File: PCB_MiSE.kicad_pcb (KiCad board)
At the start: 2 copper layers, 75 x 80.2 mm, 40 parts, among them IC1 MSP430FR2355TPT, J1 WIFI, J10 Conn_01x01, J11 Conn_01x01, J2 Conn_01x03, J3 Conn_01x01, J4 Clk read conn, J5 Conn_01x01, J6 Display, J7 Conn_01x01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

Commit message: MiSE 13/3
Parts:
- R1, R10, R5, R9: value R -> 10k
- R12, R13: value R -> 2k2
- R14, R6, R7: value R -> 1k
- R2: value R -> 31k
- R3: value R -> 20k
- R4: value R -> 47k
- moved SW1 73.1 mm to (65.5, 114.2), turned to 90 degrees
- moved C1 72.3 mm to (72.5, 111.0)
- moved R4 72.3 mm to (75.5, 111.1)
- moved R6 68.4 mm to (94.0, 43.6)
- moved SW2 67.6 mm to (82.2, 41.4), turned to 0 degrees
- moved J7 58.3 mm to (76.2, 115.0)
- moved J11 12.4 mm to (47.6, 100.8)
- moved R10 11.4 mm to (51.9, 99.0), turned to 90 degrees
- moved J1 9.99 mm to (46.3, 88.3)
- moved J10 8.01 mm to (54.6, 88.8)
- moved R5 3.25 mm to (80.8, 100.5), turned to 180 degrees
- moved C3 1.76 mm to (80.8, 94.7), turned to -90 degrees
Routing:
- net TDO/TDI: track 139.2 -> 52.6 mm, vias 3 -> 2
- net Net-(IC1-P3.4/SMCLK): track 24.7 -> 84.3 mm, vias 0 -> 1
- net U0TXD: track 50.7 -> 20.6 mm, vias 3 -> 1
- net GND: track 47.7 -> 54.4 mm
- net U0RXD: track 35.9 -> 29.2 mm, vias 2 -> 1
- net CH_EN: track 10.8 -> 5.95 mm
- net Net-(IC1-P3.1/OA2O): track 40.2 -> 37.7 mm
- net GPIOr': track 22.9 -> 23.5 mm

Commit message: Final para Gerber
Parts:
- moved J7 30.3 mm to (47.5, 105.2)
- moved J2 1.71 mm to (78.0, 105.0)
- moved R5 1.03 mm to (80.1, 101.2)
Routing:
- net TDO/TDI: track 52.6 -> 59.7 mm
- net TCK: track 18.5 -> 20.2 mm
- net Net-(IC1-P1.1/UCB0CLK/ACLK/OA0O/COMP0.1/A1): track 44.1 -> 45.1 mm
- net Net-(IC1-P3.1/OA2O): track 37.7 -> 37.0 mm
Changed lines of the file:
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@@
 	(footprint "Connector_PinHeader_2.54mm:PinHeader_1x03_P2.54mm_Vertical"
 		(layer "F.Cu")
-		(at 77.9 103.35 90)
+		(at 78.04 105.05 90)
 		(descr "Through hole straight pin header, 1x03, 2.54mm pitch, single row")
 		(tags "Through hole pin header THT 1x03 2.54mm single row")
@@
 	(footprint "Resistor_SMD:R_0805_2012Metric_Pad1.20x1.40mm_HandSolder"
 		(layer "F.Cu")
-		(at 80.85 100.5 180)
+		(at 80.08 101.19 180)
 		(descr "Resistor SMD 0805 (2012 Metric), square (rectangular) end terminal, IPC-7351 nominal with elongated pad for handsoldering. (Body size source: IPC-SM-782 page 72, https://www.pcb-3d.com/wordpress/wp-content/uploads/ipc-sm-782a_amendment_1_and_2.pdf), generated with kicad-footprint-generator")
 		(tags "resistor handsolder")
@@
 	(footprint "Connector_PinHeader_2.54mm:PinHeader_1x01_P2.54mm_Vertical"
 		(layer "F.Cu")
-		(at 76.25 114.95 90)
+		(at 47.53 105.19 90)
 		(descr "Through hole straight pin header, 1x01, 2.54mm pitch, single row")
 		(tags "Through hole pin header THT 1x01 2.54mm single row")
@@
 		(tags "Switch")
 		(property "Reference" "S1"
-			(at -2.85 7.755 0)
+			(at -1.905 3.995 0)
 			(layer "F.SilkS")
 			(effects
@@
 	)
 	(segment
+		(start 79.72 109.61)
+		(end 81.06 109.61)
+		(width 0.5)
+		(layer "F.Cu")
+		(net 13)
+	)
+	(segment
 		(start 69.95 114.2)
 		(end 69.95 107.7)
@@
 	)
 	(segment
-		(start 72.55 110.0125)
-		(end 75.4 110.0125)
+		(start 83.12 107.55)
+		(end 83.12 105.05)
 		(width 0.5)
 		(layer "F.Cu")
@@
 	)
 	(segment
-		(start 78.65 107.68)
-		(end 82.98 103.35)
+		(start 72.55 110.0125)
+		(end 75.4 110.0125)
 		(width 0.5)
 		(layer "F.Cu")
@@
 		(net 13)
 	)
+	(segment
+		(start 81.06 109.61)
+		(end 83.12 107.55)
+		(width 0.5)
+		(layer "F.Cu")
+		(net 13)
+	)
 	(via
-		(at 78.65 107.68)
+		(at 79.72 109.61)
 		(size 1)
 		(drill 0.6)
@@
 	)
 	(segment
-		(start 71.851 95.301)
-		(end 68.9 92.35)
+		(start 69.95 107.7)
+		(end 71.82 109.57)
 		(width 0.5)
 		(layer "B.Cu")
@@
 	)
 	(segment
-		(start 82.98 103.35)
-		(end 81.679 104.651)
+		(start 83.12 106.58)
+		(end 83.12 105.05)
 		(width 0.5)
 		(layer "B.Cu")
@@
 	)
 	(segment
-		(start 76.599 104.651)
-		(end 71.851 99.903)
+		(start 71.851 95.301)
+		(end 71.851 103.131)
 		(width 0.5)
 		(layer "B.Cu")
@@
 	)
 	(segment
-		(start 78.65 107.7)
-		(end 69.95 107.7)
+		(start 81.82 107.88)
+		(end 83.12 106.58)
 		(width 0.5)
 		(layer "B.Cu")
@@
 	)
 	(segment
-		(start 71.851 99.903)
-		(end 71.851 95.301)
+		(start 71.851 103.131)
+		(end 76.6 107.88)
+		(width 0.5)
+		(layer "B.Cu")
+		(net 13)
+	)
+	(segment
+		(start 79.68 109.57)
+		(end 79.72 109.61)
 		(width 0.5)
 		(layer "B.Cu")
@@
 	)
 	(segment
-		(start 78.83 107.5)
-		(end 78.65 107.68)
+		(start 68.9 92.35)
+		(end 71.851 95.301)
 		(width 0.5)
 		(layer "B.Cu")
@@
 	)
 	(segment
-		(start 81.679 104.651)
-		(end 76.599 104.651)
+		(start 71.82 109.57)
+		(end 79.68 109.57)
 		(width 0.5)
 		(layer "B.Cu")
@@
 	)
 	(segment
-		(start 78.85 107.5)
-		(end 78.83 107.5)
+		(start 76.6 107.88)
+		(end 81.82 107.88)
 		(width 0.5)
 		(layer "B.Cu")
@@
 	)
 	(segment
+		(start 79.225 100.185)
+		(end 80.57 101.53)
+		(width 0.5)
+		(layer "B.Cu")
+		(net 18)
+	)
+	(segment
 		(start 74.95 100.175)
 		(end 79.225 100.175)
@@
 	)
 	(segment
+		(start 80.58 103.46)
+		(end 80.58 105.05)
+		(width 0.5)
+		(layer "B.Cu")
+		(net 18)
+	)
+	(segment
+		(start 80.57 101.53)
+		(end 80.57 103.45)
+		(width 0.5)
+		(layer "B.Cu")
+		(net 18)
+	)
+	(segment
 		(start 79.225 100.175)
-		(end 80.74 101.69)
+		(end 79.225 100.185)
 		(width 0.5)
 		(layer "B.Cu")
@@
 	)
 	(segment
-		(start 80.74 101.69)
-		(end 80.74 103.3)
+		(start 80.57 103.45)
+		(end 80.58 103.46)
 		(width 0.5)
 		(layer "B.Cu")
@@
 	)
 	(segment
-		(start 106.84 113.8)
-		(end 103.44 110.4)
+		(start 72.85 94.45)
+		(end 72.8 94.45)
 		(width 0.5)
 		(layer "B.Cu")
@@
 	)
 	(segment
-		(start 72.85 94.45)
-		(end 72.8 94.45)
+		(start 81.35 95.2)
+		(end 73.6 95.2)
 		(width 0.5)
 		(layer "B.Cu")
@@
 	)
 	(segment
-		(start 103.44 110.4)
-		(end 96.55 110.4)
+		(start 106.84 112.01)
+		(end 105.23 110.4)
 		(width 0.5)
 		(layer "B.Cu")
@@
 	)
 	(segment
-		(start 96.55 110.4)
-		(end 81.35 95.2)
+		(start 105.23 110.4)
+		(end 96.55 110.4)
 		(width 0.5)
 		(layer "B.Cu")
@@
 	)
 	(segment
-		(start 81.35 95.2)
-		(end 73.6 95.2)
+		(start 106.84 113.8)
+		(end 106.84 112.01)
+		(width 0.5)
+		(layer "B.Cu")
+		(net 19)
+	)
+	(segment
+		(start 96.55 110.4)
+		(end 81.35 95.2)
 		(width 0.5)
 		(layer "B.Cu")
@@
 	)
 	(segment
-		(start 68.6 98.55)
-		(end 68.6 95.796)
-		(width 0.25)
-		(layer "F.Cu")
-		(net 23)
-	)
-	(segment
-		(start 75.1 102)
-		(end 76.6 100.5)
+		(start 71.19 101.14)
+		(end 79.08 101.14)
 		(width 0.5)
 		(layer "F.Cu")
@@
 	)
 	(segment
-		(start 90.65 105.5)
-		(end 94.7 105.5)
-		(width 0.5)
-		(layer "F.Cu")
-		(net 23)
-	)
-	(segment
-		(start 72.05 102)
-		(end 75.1 102)
-		(width 0.5)
-		(layer "F.Cu")
-		(net 23)
-	)
-	(segment
-		(start 86.801 101.651)
-		(end 81.001 101.651)
-		(width 0.5)
+		(start 68.6 98.55)
+		(end 68.6 95.796)
+		(width 0.25)
 		(layer "F.Cu")
 		(net 23)
 	)
 	(segment
-		(start 76.6 100.5)
-		(end 79.85 100.5)
+		(start 91.92 102.72)
+		(end 98.025 108.825)
 		(width 0.5)
 		(layer "F.Cu")
@@
 	)
 	(segment
-		(start 81.001 101.651)
-		(end 79.85 100.5)
+		(start 79.08 102.17)
+		(end 79.63 102.72)
 		(width 0.5)
 		(layer "F.Cu")
@@
 	)
 	(segment
-		(start 90.65 105.5)
-		(end 86.801 101.651)
+		(start 79.63 102.72)
+		(end 91.92 102.72)
 		(width 0.5)
 		(layer "F.Cu")
@@
 	)
 	(segment
-		(start 94.7 105.5)
-		(end 98.025 108.825)
+		(start 79.08 101.14)
+		(end 79.08 102.17)
 		(width 0.5)
 		(layer "F.Cu")
@@
 	(segment
 		(start 70.1 100.05)
-		(end 72.05 102)
+		(end 71.19 101.14)
 		(width 0.5)
 		(layer "F.Cu")

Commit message: Final para Gerber
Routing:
- net U0RXD: track 29.2 -> 22.9 mm
- net Net-(IC1-P3.4/SMCLK): track 84.3 -> 86.6 mm
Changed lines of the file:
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@@
 	)
 	(segment
-		(start 53.65 78.675)
+		(start 48 84.325)
+		(end 48.655 84.325)
+		(width 0.75)
+		(layer "B.Cu")
+		(net 1)
+	)
+	(segment
+		(start 48.655 84.325)
+		(end 53.65 79.33)
+		(width 0.75)
+		(layer "B.Cu")
+		(net 1)
+	)
+	(segment
+		(start 53.65 79.33)
 		(end 53.65 69.25)
 		(width 0.75)
@@
 	)
 	(segment
-		(start 48 84.325)
-		(end 53.65 78.675)
-		(width 0.75)
-		(layer "B.Cu")
-		(net 1)
-	)
-	(segment
 		(start 74.208 91.808)
 		(end 71.088 91.808)
@@
 	)
 	(segment
-		(start 95.976 64.474)
-		(end 95.976 48.726)
+		(start 97.12 63.33)
+		(end 97.12 47.55)
+		(width 0.5)
+		(layer "B.Cu")
+		(net 24)
+	)
+	(segment
+		(start 90.97 41.4)
+		(end 88.65 41.4)
+		(width 0.5)
+		(layer "B.Cu")
+		(net 24)
+	)
+	(segment
+		(start 70.4 90.05)
+		(end 97.12 63.33)
+		(width 0.5)
+		(layer "B.Cu")
+		(net 24)
+	)
+	(segment
+		(start 97.12 47.55)
+		(end 90.97 41.4)
 		(width 0.5)
 		(layer "B.Cu")
@@
 	)
 	(segment
-		(start 95.976 48.726)
-		(end 88.65 41.4)
-		(width 0.5)
-		(layer "B.Cu")
-		(net 24)
-	)
-	(segment
-		(start 70.4 90.05)
-		(end 95.976 64.474)
-		(width 0.5)
-		(layer "B.Cu")
-		(net 24)
-	)
-	(segment
 		(start 60.55 104)
 		(end 63.1 104)
@@
 	)
 	(segment
+		(start 55.305 90.975)
+		(end 58.775 90.975)
+		(width 0.5)
+		(layer "B.Cu")
+		(net 37)
+	)
+	(segment
 		(start 54.6 88.85)
 		(end 51.9 86.15)
@@
 	)
 	(segment
-		(start 50.149 86.999)
-		(end 47.561 86.999)
+		(start 50.17 86.15)
+		(end 48.41 86.15)
 		(width 0.5)
 		(layer "B.Cu")
@@
 	)
 	(segment
-		(start 58.775 90.975)
-		(end 54.125 90.975)
+		(start 54.6 90.27)
+		(end 55.305 90.975)
+		(width 0.5)
+		(layer "B.Cu")
+		(net 37)
+	)
+	(segment
+		(start 48.41 86.15)
+		(end 47.17 86.15)
 		(width 0.5)
 		(layer "B.Cu")
@@
 	)
 	(segment
-		(start 47.561 86.999)
+		(start 46.26 87.06)
 		(end 46.26 88.3)
 		(width 0.5)
@@
 	)
 	(segment
-		(start 48.41 86.15)
-		(end 46.26 88.3)
+		(start 47.17 86.15)
+		(end 46.26 87.06)
 		(width 0.5)
 		(layer "B.Cu")
@@
 	)
 	(segment
-		(start 54.125 90.975)
-		(end 50.149 86.999)
-		(width 0.5)
-		(layer "B.Cu")
+		(start 54.6 88.85)
+		(end 54.6 90.27)
+		(width 0.5)
+		(layer "B.Cu")

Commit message: Final para Gerber
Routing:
- net U0RXD: track 22.9 -> 21.1 mm
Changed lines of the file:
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@@
-	)
-	(segment
-		(start 50.17 86.15)
-		(end 48.41 86.15)
-		(width 0.5)
-		(layer "B.Cu")
-		(net 37)
 	)
 	(segment

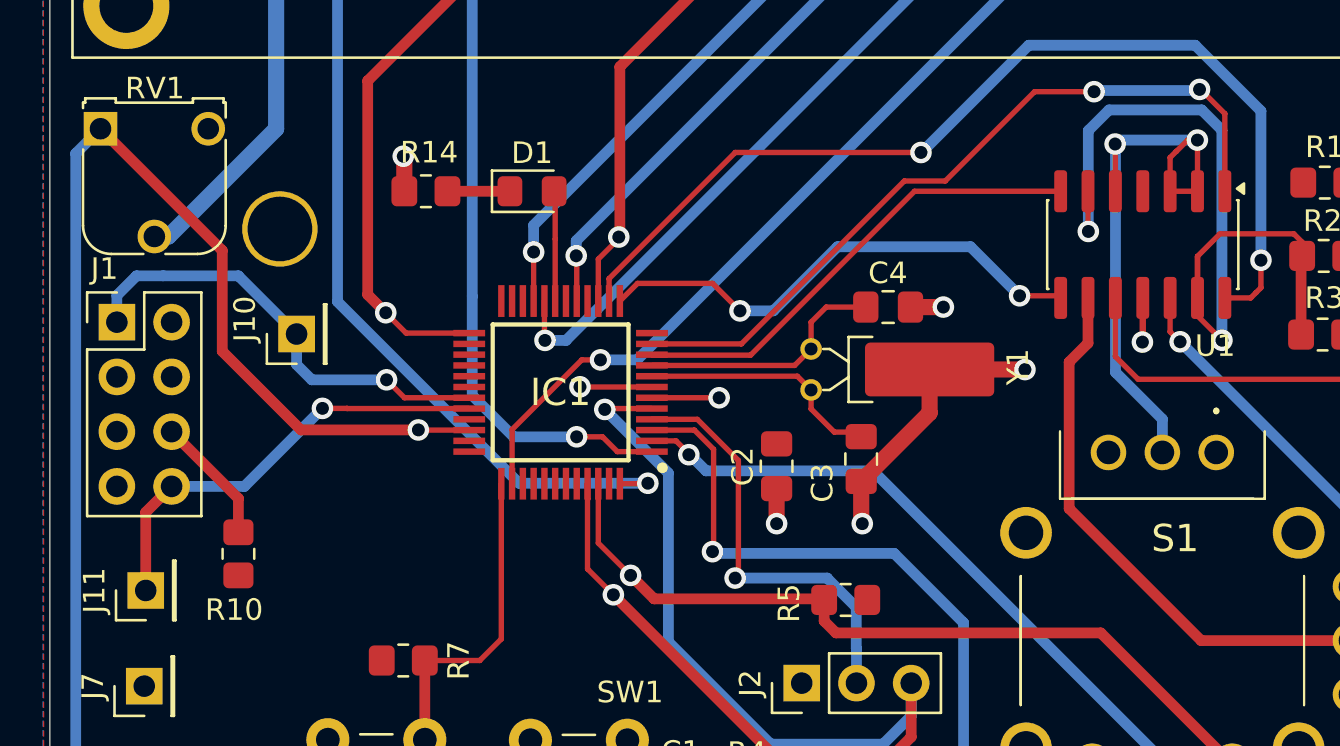
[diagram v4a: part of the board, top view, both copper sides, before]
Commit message: Cambios de errores opamp
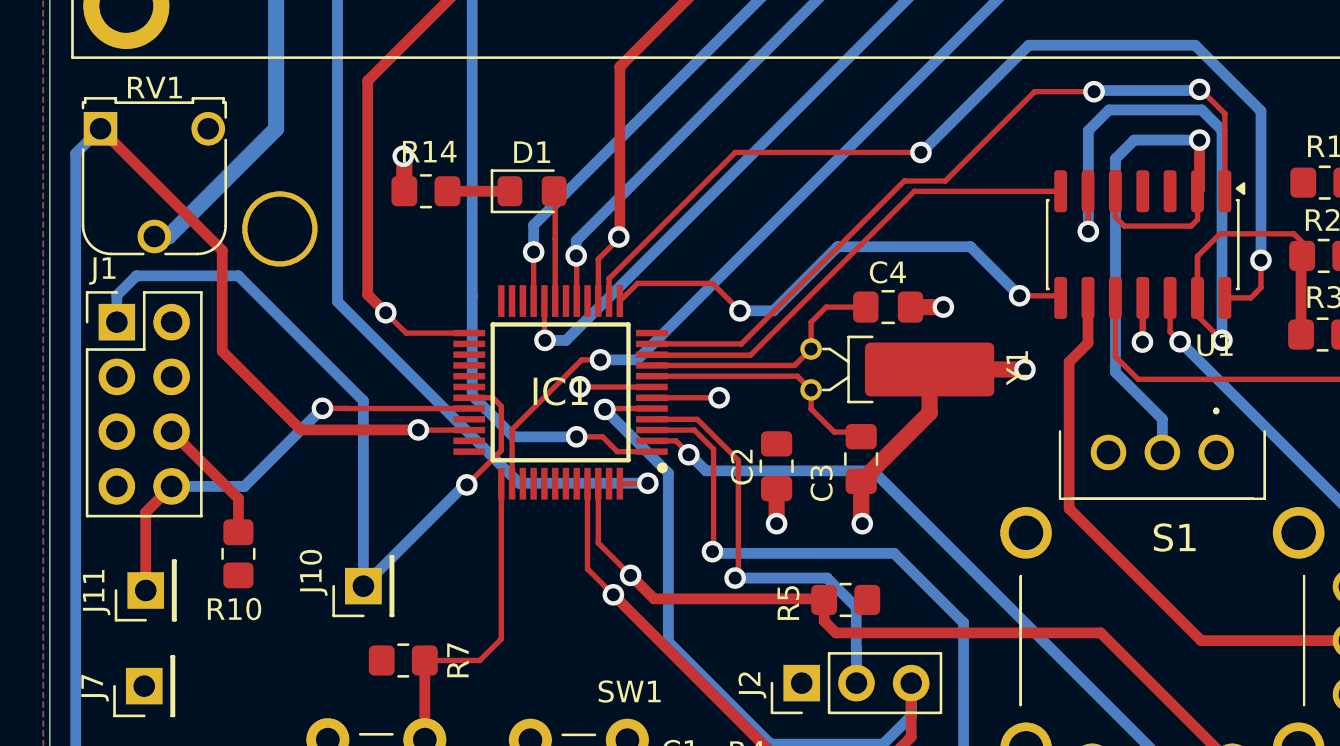
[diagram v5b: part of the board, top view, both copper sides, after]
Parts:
- C3, C4: value 100n -> 12p
- moved J10 12.1 mm to (57.7, 100.5)
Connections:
- S1 pad 2: Net-(U1A-+) -> Net-(U1A--)
- U1 pad 2: Net-(U1A-+) -> Net-(U1A--)
- U1 pad 3: Net-(U1A-+) -> VCC
- U1 pad 5: Net-(U1A-+) -> Net-(U1A--)
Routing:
- net Net-(U1A-+): track 28.7 -> 0.00 mm, vias 2 -> 0
- net Net-(U1A--): track 0.00 -> 27.9 mm, vias 0 -> 1
- net U0RXD: track 21.1 -> 36.8 mm
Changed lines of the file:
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@@
 	(net 29 "Net-(IC1-P3.2{slash}OA2-)")
 	(net 30 "Net-(S1-2')")
-	(net 31 "Net-(U1A-+)")
+	(net 31 "Net-(U1A--)")
 	(net 32 "GPIOl'")
 	(net 33 "GPIOr'")
@@
 			)
 		)
-		(property "Value" "100n"
+		(property "Value" "12p"
 			(at 0 1.68 0)
 			(layer "F.Fab")
@@
 			)
 		)
-		(property "Value" "100n"
+		(property "Value" "12p"
 			(at 0 1.68 90)
 			(layer "F.Fab")
@@
 			(layers "F.Cu" "F.Mask" "F.Paste")
 			(roundrect_rratio 0.25)
-			(net 31 "Net-(U1A-+)")
+			(net 31 "Net-(U1A--)")
 			(pinfunction "-")
 			(pintype "input")
@@
 			(layers "F.Cu" "F.Mask" "F.Paste")
 			(roundrect_rratio 0.25)
-			(net 31 "Net-(U1A-+)")
+			(net 2 "VCC")
 			(pinfunction "+")
 			(pintype "input")
@@
 			(layers "F.Cu" "F.Mask" "F.Paste")
 			(roundrect_rratio 0.25)
-			(net 31 "Net-(U1A-+)")
+			(net 31 "Net-(U1A--)")
 			(pinfunction "+")
 			(pintype "input")
@@
 			(layers "*.Cu" "*.Mask")
 			(remove_unused_layers no)
-			(net 31 "Net-(U1A-+)")
+			(net 31 "Net-(U1A--)")
 			(pinfunction "2")
 			(pintype "passive")
@@
 	(footprint "Connector_PinHeader_2.54mm:PinHeader_1x01_P2.54mm_Vertical"
 		(layer "F.Cu")
-		(at 54.6 88.85 90)
+		(at 57.7 100.55 90)
 		(descr "Through hole straight pin header, 1x01, 2.54mm pitch, single row")
 		(tags "Through hole pin header THT 1x01 2.54mm single row")
@@
 	)
 	(segment
-		(start 96.4 79.85)
-		(end 96.4 80.2)
-		(width 0.25)
-		(layer "F.Cu")
-		(net 31)
-	)
-	(segment
-		(start 95.42 80.375)
-		(end 95.425 80.375)
-		(width 0.25)
-		(layer "F.Cu")
-		(net 31)
-	)
-	(segment
-		(start 96.4 79.85)
-		(end 96.288206 79.961794)
-		(width 0.25)
+		(start 96.5 79.85)
+		(end 96.5 82.13)
+		(width 0.5)
 		(layer "F.Cu")
 		(net 31)
 	)
 	(segment
-		(start 96.405 79.855)
-		(end 96.4 79.85)
+		(start 96.41 83.54)
+		(end 96.11 83.84)
 		(width 0.25)
 		(layer "F.Cu")
@@
 	)
 	(segment
-		(start 95.135 82.225)
-		(end 95.135 80.66)
-		(width 0.25)
-		(layer "F.Cu")
-		(net 31)
-	)
-	(segment
-		(start 92.583364 80.443364)
-		(end 92.595 80.455)
-		(width 0.25)
-		(layer "F.Cu")
-		(net 31)
-	)
-	(segment
-		(start 96.405 82.225)
-		(end 96.405 79.855)
+		(start 93.01 83.84)
+		(end 92.595 83.425)
 		(width 0.25)
 		(layer "F.Cu")
@@
 	)
 	(segment
-		(start 92.583364 80.033364)
-		(end 92.583364 80.443364)
+		(start 92.595 83.425)
+		(end 92.595 82.225)
 		(width 0.25)
 		(layer "F.Cu")
@@
 	)
 	(segment
-		(start 95.135 80.66)
-		(end 95.42 80.375)
-		(width 0.25)
+		(start 96.5 82.13)
+		(end 96.405 82.225)
+		(width 0.5)
 		(layer "F.Cu")
 		(net 31)
 	)
 	(segment
-		(start 95.135 82.225)
-		(end 96.405 82.225)
+		(start 96.405 82.225)
+		(end 96.405 83.199999)
 		(width 0.25)
 		(layer "F.Cu")
@@
 	)
 	(segment
-		(start 92.595 80.455)
-		(end 92.595 82.225)
+		(start 96.405 83.199999)
+		(end 96.41 83.204999)
 		(width 0.25)
 		(layer "F.Cu")
@@
 	)
 	(segment
-		(start 95.425 80.375)
-		(end 95.95 79.85)
+		(start 96.11 83.84)
+		(end 93.01 83.84)
 		(width 0.25)
 		(layer "F.Cu")
@@
 	)
 	(segment
-		(start 95.95 79.85)
-		(end 96.4 79.85)
+		(start 96.41 83.204999)
+		(end 96.41 83.54)
 		(width 0.25)
 		(layer "F.Cu")
@@
 	)
 	(via
-		(at 96.4 79.85)
-		(size 1)
-		(drill 0.6)
-		(layers "F.Cu" "B.Cu")
-		(net 31)
-	)
-	(via
-		(at 92.583364 80.033364)
+		(at 96.5 79.85)
 		(size 1)
 		(drill 0.6)
@@
 	)
 	(segment
-		(start 92.583364 80.033364)
-		(end 92.6 80.05)
-		(width 0.5)
-		(layer "B.Cu")
-		(net 31)
-	)
-	(segment
-		(start 92.6 80.05)
-		(end 92.6 90.625)
+		(start 92.6 80.72)
+		(end 93.47 79.85)
 		(width 0.5)
 		(layer "B.Cu")
@@
 	)
 	(segment
-		(start 92.6 90.625)
+		(start 94.775 94.345)
 		(end 94.775 92.8)
 		(width 0.5)
@@
 	(segment
 		(start 94.775 92.8)
-		(end 94.775 94.345)
+		(end 92.6 90.625)
 		(width 0.5)
 		(layer "B.Cu")
@@
 	)
 	(segment
-		(start 96.4 79.85)
-		(end 92.766728 79.85)
+		(start 93.47 79.85)
+		(end 96.5 79.85)
 		(width 0.5)
 		(layer "B.Cu")
@@
 	)
 	(segment
-		(start 92.766728 79.85)
-		(end 92.583364 80.033364)
+		(start 92.6 90.625)
+		(end 92.6 80.72)
 		(width 0.5)
 		(layer "B.Cu")
@@
 	)
 	(segment
-		(start 59.608 91.808)
-		(end 62.612 91.808)
+		(start 63.708 91.808)
+		(end 64.1 92.2)
+		(width 0.25)
+		(layer "F.Cu")
+		(net 37)
+	)
+	(segment
+		(start 64.1 94.2565)
+		(end 62.5065 95.85)
+		(width 0.25)
+		(layer "F.Cu")
+		(net 37)
+	)
+	(segment
+		(start 62.5065 95.85)
+		(end 62.5 95.85)
+		(width 0.25)
+		(layer "F.Cu")
+		(net 37)
+	)
+	(segment
+		(start 64.1 92.2)
+		(end 64.1 94.2565)
 		(width 0.25)
 		(layer "F.Cu")
@@
 	)
 	(segment
-		(start 58.775 90.975)
-		(end 59.608 91.808)
+		(start 62.612 91.808)
+		(end 63.708 91.808)
 		(width 0.25)
 		(layer "F.Cu")
@@
 	)
 	(via
-		(at 58.775 90.975)
+		(at 62.5 95.85)
 		(size 1)
 		(drill 0.6)
@@
 	)
 	(segment
-		(start 55.305 90.975)
-		(end 58.775 90.975)
+		(start 57.7 91.95)
+		(end 57.7 100.55)
 		(width 0.5)
 		(layer "B.Cu")
@@
 	)
 	(segment
-		(start 54.6 88.85)
+		(start 47.17 86.15)
 		(end 51.9 86.15)
 		(width 0.5)
@@
 	)
 	(segment
-		(start 54.6 90.27)
-		(end 55.305 90.975)
+		(start 57.7 100.55)
+		(end 62.4 95.85)
 		(width 0.5)
 		(layer "B.Cu")
@@
 	)
 	(segment
-		(start 48.41 86.15)
-		(end 47.17 86.15)
-		(width 0.5)
-		(layer "B.Cu")
-		(net 37)
-	)
-	(segment
-		(start 51.9 86.15)
-		(end 48.41 86.15)
+		(start 46.26 88.3)
+		(end 46.26 87.06)
 		(width 0.5)
 		(layer "B.Cu")
@@
 	(segment
 		(start 46.26 87.06)
-		(end 46.26 88.3)
+		(end 47.17 86.15)
 		(width 0.5)
 		(layer "B.Cu")
@@
 	)
 	(segment
-		(start 47.17 86.15)
-		(end 46.26 87.06)
+		(start 51.9 86.15)
+		(end 57.7 91.95)
 		(width 0.5)
 		(layer "B.Cu")
@@
 	)
 	(segment
-		(start 54.6 88.85)
-		(end 54.6 90.27)
+		(start 62.4 95.85)
+		(end 62.5 95.85)
 		(width 0.5)
 		(layer "B.Cu")

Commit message: Agrego gerbers y correcciones
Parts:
- removed SW4: SW_Push, Button_Switch_THT:SW_PUSH_6mm
- C3, C4: value 12p -> 100n
- moved R9 44.6 mm to (53.7, 79.7)
- moved R6 4.63 mm to (89.6, 42.3)
- moved SW2 4.40 mm to (77.8, 41.2)
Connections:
- IC1 pad 30: unconnected-(IC1-P2.0/TB1.1/COMP0.O-Pad30) -> Net-(IC1-P2.0/TB1.1/COMP0.O)
- J6 pad 5: Net-(J6-Pin_5) -> Net-(IC1-P2.0/TB1.1/COMP0.O)
- R9 pad 2: Net-(J6-Pin_5) -> Net-(IC1-P2.0/TB1.1/COMP0.O)
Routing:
- net Net-(IC1-P2.0/TB1.1/COMP0.O): track 0.00 -> 45.0 mm, vias 0 -> 1
- net Net-(J6-Pin_5): track 43.1 -> 0.00 mm
- net Net-(IC1-P3.4/SMCLK): track 86.6 -> 90.6 mm
